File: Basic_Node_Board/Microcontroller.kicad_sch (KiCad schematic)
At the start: 35 parts, among them J1 Conn_01x02, J2 Conn_01x19_Socket, J3 Conn_01x19_Socket, J4 Conn_01x02_Pin, U2 ESP32-DEVKIT-C, U3 TPS54560BQDDARQ1, U4 AP64060WU-7, U5 AP64060WU-7, U6 TJA1050T/CM,118

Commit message: fixed routing under the lora board module
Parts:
- J1: footprint Connector_PinSocket_1.00mm:PinSocket_1x02_P1.00mm_Vertical -> Connector_PinHeader_1.27mm:PinHeader_1x02_P1.27mm_Horizontal
- J4: footprint Connector_PinSocket_1.00mm:PinSocket_1x02_P1.00mm_Vertical -> Connector_PinHeader_1.00mm:PinHeader_1x02_P1.00mm_Horizontal
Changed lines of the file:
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@@
 			)
 		)
-		(property "Footprint" "Connector_PinSocket_1.00mm:PinSocket_1x02_P1.00mm_Vertical"
+		(property "Footprint" "Connector_PinHeader_1.27mm:PinHeader_1x02_P1.27mm_Horizontal"
 			(at 26.67 49.53 0)
 			(effects
@@
 			)
 		)
-		(property "Footprint" "Connector_PinSocket_1.00mm:PinSocket_1x02_P1.00mm_Vertical"
+		(property "Footprint" "Connector_PinHeader_1.00mm:PinHeader_1x02_P1.00mm_Horizontal"
 			(at 276.86 139.7 0)
 			(effects

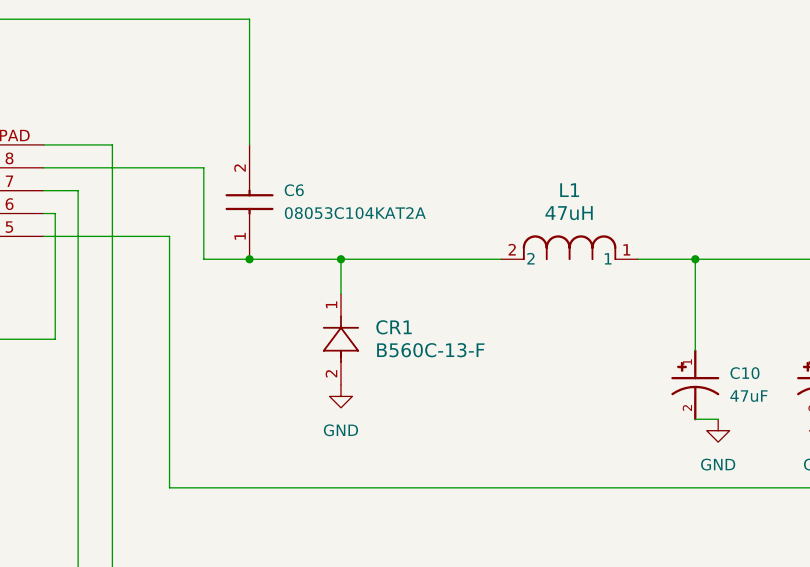
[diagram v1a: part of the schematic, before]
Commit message: verified all componnents are 1206 for SMD
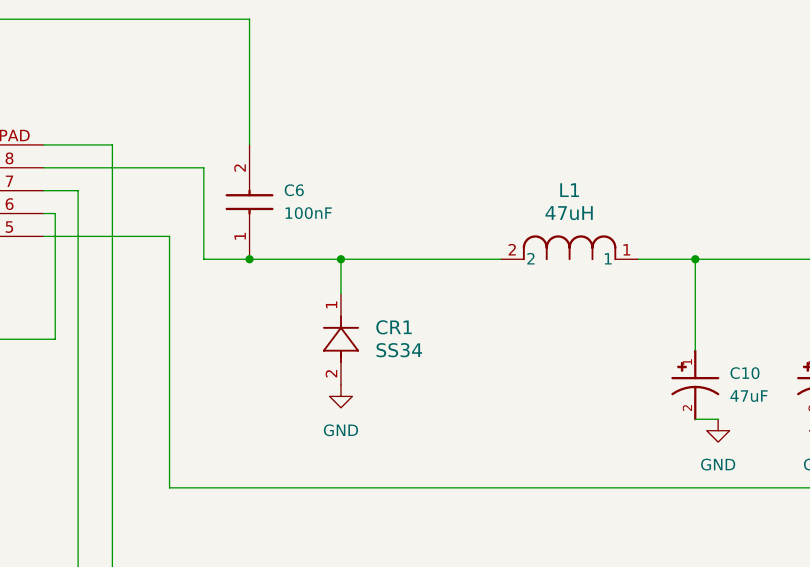
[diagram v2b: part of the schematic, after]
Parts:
- C10, C11: footprint Capacitor_SMD:C_0402_1005Metric_Pad0.74x0.62mm_HandSolder -> Capacitor_SMD:C_1206_3216Metric_Pad1.33x1.80mm_HandSolder
- C3, C4: footprint Capacitor_SMD:C_0504_1310Metric_Pad0.83x1.28mm_HandSolder -> Capacitor_SMD:C_1206_3216Metric_Pad1.33x1.80mm_HandSolder
- C5: footprint Capacitor_SMD:C_0603_1608Metric_Pad1.08x0.95mm_HandSolder -> Capacitor_SMD:C_1206_3216Metric_Pad1.33x1.80mm_HandSolder
- C6: value 08053C104KAT2A -> 100nF; footprint Capacitor_SMD:C_0504_1310Metric_Pad0.83x1.28mm_HandSolder -> Capacitor_SMD:C_1206_3216Metric_Pad1.33x1.80mm_HandSolder
- CR1: value B560C-13-F -> SS34; footprint Diode_SMD:D_0201_0603Metric_Pad0.64x0.40mm_HandSolder -> Diode_SMD:D_1206_3216Metric_Pad1.42x1.75mm_HandSolder
- J1: footprint Connector_PinHeader_1.27mm:PinHeader_1x02_P1.27mm_Horizontal -> Connector_PinSocket_1.00mm:PinSocket_1x02_P1.00mm_Vertical
- J4: footprint Connector_PinHeader_1.00mm:PinHeader_1x02_P1.00mm_Horizontal -> Connector_PinSocket_1.00mm:PinSocket_1x02_P1.00mm_Vertical
- L1: footprint Inductor_SMD:L_0201_0603Metric_Pad0.64x0.40mm_HandSolder -> Inductor_SMD:L_1206_3216Metric_Pad1.22x1.90mm_HandSolder
- R1, R11, R12, R3: footprint Resistor_SMD:R_0201_0603Metric_Pad0.64x0.40mm_HandSolder -> Resistor_SMD:R_1206_3216Metric_Pad1.30x1.75mm_HandSolder
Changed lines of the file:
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@@
 			)
 		)
-		(property "Footprint" "Resistor_SMD:R_0201_0603Metric_Pad0.64x0.40mm_HandSolder"
+		(property "Footprint" "Resistor_SMD:R_1206_3216Metric_Pad1.30x1.75mm_HandSolder"
 			(at 100.33 69.85 0)
 			(effects
@@
 			)
 		)
-		(property "Value" "B560C-13-F"
+		(property "Value" "SS34"
 			(at 184.15 57.1499 90)
 			(effects
@@
 			)
 		)
-		(property "Footprint" "Diode_SMD:D_0201_0603Metric_Pad0.64x0.40mm_HandSolder"
+		(property "Footprint" "Diode_SMD:D_1206_3216Metric_Pad1.42x1.75mm_HandSolder"
 			(at 180.34 60.96 0)
 			(effects
@@
 			)
 		)
-		(property "Footprint" "Capacitor_SMD:C_0504_1310Metric_Pad0.83x1.28mm_HandSolder"
+		(property "Footprint" "Capacitor_SMD:C_1206_3216Metric_Pad1.33x1.80mm_HandSolder"
 			(at 60.96 85.09 0)
 			(effects
@@
 			)
 		)
-		(property "Footprint" "Capacitor_SMD:C_0603_1608Metric_Pad1.08x0.95mm_HandSolder"
+		(property "Footprint" "Capacitor_SMD:C_1206_3216Metric_Pad1.33x1.80mm_HandSolder"
 			(at 74.93 72.39 0)
 			(effects
@@
 			)
 		)
-		(property "Footprint" "Resistor_SMD:R_0201_0603Metric_Pad0.64x0.40mm_HandSolder"
+		(property "Footprint" "Resistor_SMD:R_1206_3216Metric_Pad1.30x1.75mm_HandSolder"
 			(at 60.96 66.04 0)
 			(effects
@@
 			)
 		)
-		(property "Footprint" "Capacitor_SMD:C_0504_1310Metric_Pad0.83x1.28mm_HandSolder"
+		(property "Footprint" "Capacitor_SMD:C_1206_3216Metric_Pad1.33x1.80mm_HandSolder"
 			(at 44.45 48.26 0)
 			(effects
@@
 			)
 		)
-		(property "Footprint" "Resistor_SMD:R_0201_0603Metric_Pad0.64x0.40mm_HandSolder"
+		(property "Footprint" "Resistor_SMD:R_1206_3216Metric_Pad1.30x1.75mm_HandSolder"
 			(at 246.38 87.63 0)
 			(effects
@@
 			)
 		)
-		(property "Footprint" "Inductor_SMD:L_0201_0603Metric_Pad0.64x0.40mm_HandSolder"
+		(property "Footprint" "Inductor_SMD:L_1206_3216Metric_Pad1.22x1.90mm_HandSolder"
 			(at 198.12 46.99 0)
 			(effects
@@
 			)
 		)
-		(property "Footprint" "Capacitor_SMD:C_0402_1005Metric_Pad0.74x0.62mm_HandSolder"
+		(property "Footprint" "Capacitor_SMD:C_1206_3216Metric_Pad1.33x1.80mm_HandSolder"
 			(at 219.71 62.23 0)
 			(effects
@@
 			)
 		)
-		(property "Value" "08053C104KAT2A"
+		(property "Value" "100nF"
 			(at 173.99 41.9099 90)
 			(effects
@@
 			)
 		)
-		(property "Footprint" "Capacitor_SMD:C_0504_1310Metric_Pad0.83x1.28mm_HandSolder"
+		(property "Footprint" "Capacitor_SMD:C_1206_3216Metric_Pad1.33x1.80mm_HandSolder"
 			(at 266.37 38.1 0)
 			(effects
@@
 			)
 		)
-		(property "Footprint" "Capacitor_SMD:C_0402_1005Metric_Pad0.74x0.62mm_HandSolder"
+		(property "Footprint" "Capacitor_SMD:C_1206_3216Metric_Pad1.33x1.80mm_HandSolder"
 			(at 233.68 62.23 0)
 			(effects
@@
 			)
 		)
-		(property "Footprint" "Resistor_SMD:R_0201_0603Metric_Pad0.64x0.40mm_HandSolder"
+		(property "Footprint" "Resistor_SMD:R_1206_3216Metric_Pad1.30x1.75mm_HandSolder"
 			(at 246.38 60.96 0)
 			(effects
@@
 			)
 		)
-		(property "Footprint" "Connector_PinHeader_1.27mm:PinHeader_1x02_P1.27mm_Horizontal"
+		(property "Footprint" "Connector_PinSocket_1.00mm:PinSocket_1x02_P1.00mm_Vertical"
 			(at 26.67 49.53 0)
 			(effects
@@
 			)
 		)
-		(property "Footprint" "Connector_PinHeader_1.00mm:PinHeader_1x02_P1.00mm_Horizontal"
+		(property "Footprint" "Connector_PinSocket_1.00mm:PinSocket_1x02_P1.00mm_Vertical"
 			(at 276.86 139.7 0)
 			(effects

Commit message: reverified pin headers for canbus and power
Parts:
- J1, J4: footprint Connector_PinSocket_1.00mm:PinSocket_1x02_P1.00mm_Vertical -> Connector_PinHeader_1.00mm:PinHeader_1x02_P1.00mm_Vertical
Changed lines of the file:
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@@
 			)
 		)
-		(property "Footprint" "Connector_PinSocket_1.00mm:PinSocket_1x02_P1.00mm_Vertical"
+		(property "Footprint" "Connector_PinHeader_1.00mm:PinHeader_1x02_P1.00mm_Vertical"
 			(at 26.67 49.53 0)
 			(effects
@@
 			)
 		)
-		(property "Footprint" "Connector_PinSocket_1.00mm:PinSocket_1x02_P1.00mm_Vertical"
+		(property "Footprint" "Connector_PinHeader_1.00mm:PinHeader_1x02_P1.00mm_Vertical"
 			(at 276.86 139.7 0)
 			(effects
